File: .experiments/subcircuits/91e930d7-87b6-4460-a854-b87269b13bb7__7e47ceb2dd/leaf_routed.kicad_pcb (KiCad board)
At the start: 2 copper layers, 34.9 x 18.6 mm, 13 parts, among them U2 BQ24072

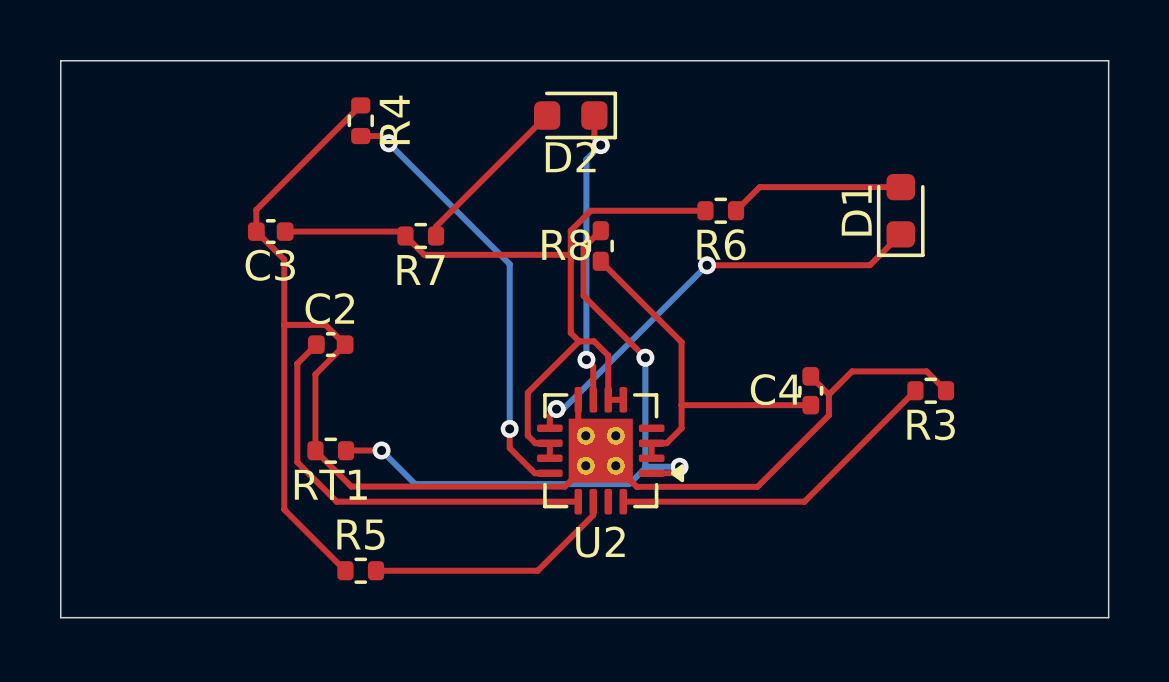
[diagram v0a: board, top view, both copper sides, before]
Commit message: feat: parent board stamping with preserved child copper
- Add --pcb, --stamp, --route, --jar flags to compose_subcircuits.py
- Implement subprocess-based parent board stamping (no pcbnew in main process)
- Add _stamp_parent_board() that copies base PCB, moves footprints to
  composed positions, clears existing tracks/zones, recreates child copper
  traces and vias with proper net name resolution
- Add _route_parent_board() for FreeRouting with preserve_existing_copper
- Add _persist_parent_artifact() for parent solved_layout.json persistence
- Store ParentComposition on ParentCompositionState for downstream access
- Update leaf artifacts from fresh pipeline run (6/6 leaves routed)
- Parent stamp verified: 37 components, 286 child traces, 10 vias preserved
  on real .kicad_pcb board with correct positions and net assignments
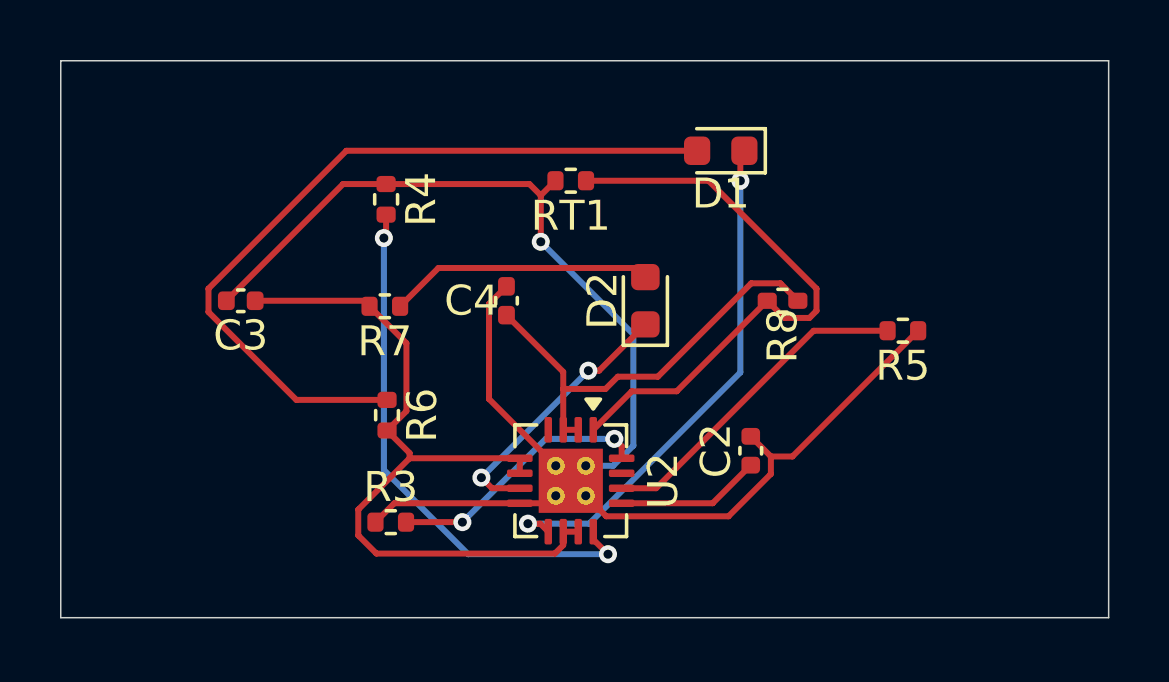
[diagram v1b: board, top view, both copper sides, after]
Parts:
- moved R5 19.8 mm to (28.1, 9.00), turned to 180 degrees
- moved R3 18.5 mm to (11.0, 15.4), turned to 0 degrees
- moved C2 14.4 mm to (23.0, 13.0), turned to 90 degrees
- moved R6 13.0 mm to (10.9, 11.8), turned to -90 degrees
- moved RT1 12.0 mm to (17.0, 4.00)
- moved C4 10.6 mm to (14.9, 8.00)
- moved D2 6.66 mm to (19.5, 8.00), turned to 90 degrees
- moved R8 6.33 mm to (24.1, 8.00), turned to 180 degrees
- moved D1 6.32 mm to (22.0, 3.00), turned to 180 degrees
- moved R4 2.75 mm to (10.8, 4.62)
- moved R7 2.63 mm to (10.8, 8.19)
- moved C3 2.51 mm to (6.00, 8.00)
- moved U2 1.41 mm to (17.0, 14.0), turned to -90 degrees
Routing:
- net Net-(D1-A): track 5.82 -> 26.1 mm
- net /VBUS: track 14.1 -> 4.83 mm
- net Net-(U2-ILIM): track 14.6 -> 18.1 mm
- net Net-(D2-A): track 5.55 -> 8.83 mm
- net GND: track 53.5 -> 56.7 mm, vias 0 -> 1
- net /CHG_N: track 14.6 -> 17.4 mm
- net Net-(U2-TMR): track 8.46 -> 11.0 mm
- net Net-(U2-ISET): track 11.3 -> 8.84 mm, vias 0 -> 2
- net /NTC_SENSE: track 21.8 -> 19.5 mm, vias 3 -> 0
- net /VBAT: track 12.7 -> 14.6 mm
- net /VSYS: track 26.7 -> 25.6 mm
- net Net-(D2-K): track 9.86 -> 9.01 mm

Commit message: feat: unified hierarchical solver (solve_hierarchy.py)
Single-command entry point for the full subcircuit pipeline:
  python3 solve_hierarchy.py LLUPS.kicad_sch --pcb LLUPS.kicad_pcb --route

Phase 1: Solve leaf subcircuits (delegates to solve_subcircuits.py)
  - 6 leaves solved and routed via FreeRouting
  - Canonical copper persisted in solved_layout.json

Phase 2: Compose and route parent (delegates to compose_subcircuits.py)
  - Grid layout of 6 children with 5mm spacing
  - Child copper preserved on stamped parent board
  - FreeRouting routes interconnect nets between subcircuits
  - Parent artifact persisted with full copper

Flags: --skip-leaves, --leaf-only, --rounds, --mode, --spacing-mm, --jar
Full pipeline completes in ~4 minutes (with routing)
Skip-leaves mode completes in ~28 seconds
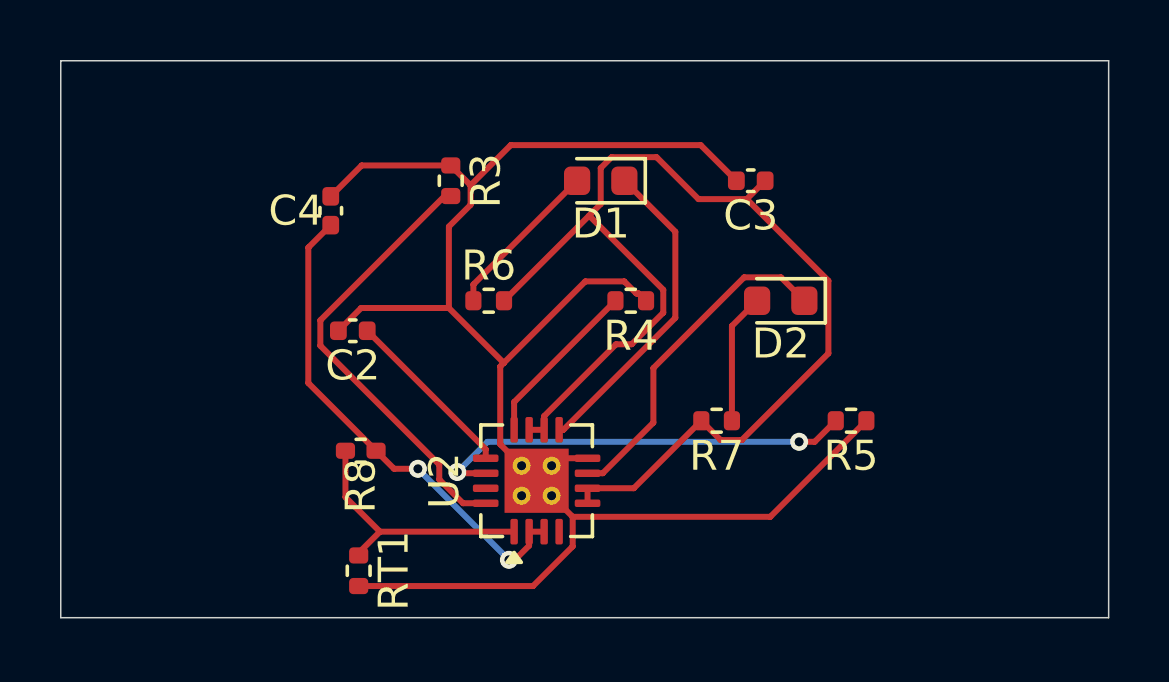
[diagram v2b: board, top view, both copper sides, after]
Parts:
- moved C3 17.5 mm to (23.0, 4.00)
- moved R8 14.9 mm to (10.0, 13.0)
- moved RT1 14.8 mm to (9.93, 17.0), turned to -90 degrees
- moved C2 13.9 mm to (9.73, 9.00), turned to 180 degrees
- moved R7 11.7 mm to (21.9, 12.0)
- moved R3 11.6 mm to (13.0, 4.00), turned to -90 degrees
- moved R4 8.83 mm to (19.0, 8.00), turned to 180 degrees
- moved C4 6.58 mm to (9.00, 5.00)
- moved R6 5.10 mm to (14.3, 8.00), turned to 0 degrees
- moved D2 4.51 mm to (24.0, 8.00), turned to 180 degrees
- moved D1 4.12 mm to (18.0, 4.00)
- moved R5 3.46 mm to (26.3, 12.0)
- moved U2 1.14 mm to (15.9, 14.0), turned to 90 degrees
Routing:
- net Net-(D1-A): track 26.1 -> 5.43 mm
- net /VSYS: track 25.6 -> 40.0 mm
- net Net-(U2-ILIM): track 18.1 -> 5.70 mm, vias 2 -> 0
- net /NTC_SENSE: track 19.5 -> 8.73 mm
- net /CHG_N: track 17.4 -> 10.7 mm, vias 2 -> 0
- net Net-(U2-ISET): track 8.84 -> 14.9 mm, vias 2 -> 0
- net GND: track 56.7 -> 61.8 mm, vias 1 -> 0
- net Net-(D2-A): track 8.83 -> 4.35 mm
- net Net-(U2-TMR): track 11.0 -> 14.3 mm, vias 0 -> 2
- net Net-(D2-K): track 9.01 -> 11.3 mm, vias 2 -> 0
- net /VBAT: track 14.6 -> 16.5 mm, vias 0 -> 2
- net /VBUS: track 4.83 -> 5.89 mm
